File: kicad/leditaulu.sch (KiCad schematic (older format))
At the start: 45 parts, among them CON1 12V input, P1 Programming header, P2 I2C addr select, P4 I2C addr select, P5 Interconnect 1, P6 Interconnect 2, SW1 SW_SPST, SW2 SW_SPST, U1 ESP-12E, U2 TLC59116IPWR, U3 LD1086, U4 nRF24L01+, U5 TLC59116IPWR

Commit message: Fix submodules (ESP8266)
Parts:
- U1: footprint ESP8266:ESP-12E -> ESP8266:ESP-12E_SMD
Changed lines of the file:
@@
 F 0 "U1" H 2625 1350 50  0000 C CNN
 F 1 "ESP-12E" H 2625 1550 50  0000 C CNN
-F 2 "ESP8266:ESP-12E" H 2625 1450 50  0001 C CNN
+F 2 "ESP8266:ESP-12E_SMD" H 2625 1450 50  0001 C CNN
 F 3 "" H 2625 1450 50  0001 C CNN
 	1    2625 1450
@@
 ESP_GPIO0
 $Comp
-L Earth #PWR26
+L Earth #PWR01
 U 1 1 58EA62EF
 P 10375 1000
-F 0 "#PWR26" H 10375 750 50  0001 C CNN
+F 0 "#PWR01" H 10375 750 50  0001 C CNN
 F 1 "Earth" H 10375 850 50  0001 C CNN
 F 2 "" H 10375 1000 50  0000 C CNN
@@
 $EndComp
 $Comp
-L Earth #PWR27
+L Earth #PWR02
 U 1 1 58EA6329
 P 10375 1500
-F 0 "#PWR27" H 10375 1250 50  0001 C CNN
+F 0 "#PWR02" H 10375 1250 50  0001 C CNN
 F 1 "Earth" H 10375 1350 50  0001 C CNN
 F 2 "" H 10375 1500 50  0000 C CNN
@@
 3V3
 $Comp
-L Earth #PWR9
+L Earth #PWR03
 U 1 1 58EA6BBD
 P 3525 1850
-F 0 "#PWR9" H 3525 1600 50  0001 C CNN
+F 0 "#PWR03" H 3525 1600 50  0001 C CNN
 F 1 "Earth" H 3525 1700 50  0001 C CNN
 F 2 "" H 3525 1850 50  0000 C CNN
@@
 $EndComp
 $Comp
-L Earth #PWR5
+L Earth #PWR04
 U 1 1 58EA6CA7
 P 1200 2050
-F 0 "#PWR5" H 1200 1800 50  0001 C CNN
+F 0 "#PWR04" H 1200 1800 50  0001 C CNN
 F 1 "Earth" H 1200 1900 50  0001 C CNN
 F 2 "" H 1200 2050 50  0000 C CNN
@@
 $EndComp
 $Comp
-L Earth #PWR8
+L Earth #PWR05
 U 1 1 58EBE920
 P 2400 4300
-F 0 "#PWR8" H 2400 4050 50  0001 C CNN
+F 0 "#PWR05" H 2400 4050 50  0001 C CNN
 F 1 "Earth" H 2400 4150 50  0001 C CNN
 F 2 "" H 2400 4300 50  0000 C CNN
@@
 $EndComp
 $Comp
-L Earth #PWR11
+L Earth #PWR06
 U 1 1 58EBE9BE
 P 4100 3800
-F 0 "#PWR11" H 4100 3550 50  0001 C CNN
+F 0 "#PWR06" H 4100 3550 50  0001 C CNN
 F 1 "Earth" H 4100 3650 50  0001 C CNN
 F 2 "" H 4100 3800 50  0000 C CNN
@@
 $EndComp
 $Comp
-L Earth #PWR12
+L Earth #PWR07
 U 1 1 58EBE9F7
 P 4100 4300
-F 0 "#PWR12" H 4100 4050 50  0001 C CNN
+F 0 "#PWR07" H 4100 4050 50  0001 C CNN
 F 1 "Earth" H 4100 4150 50  0001 C CNN
 F 2 "" H 4100 4300 50  0000 C CNN
@@
 $EndComp
 $Comp
-L Earth #PWR13
+L Earth #PWR08
 U 1 1 58EBEB42
 P 4250 3075
-F 0 "#PWR13" H 4250 2825 50  0001 C CNN
+F 0 "#PWR08" H 4250 2825 50  0001 C CNN
 F 1 "Earth" H 4250 2925 50  0001 C CNN
 F 2 "" H 4250 3075 50  0000 C CNN
@@
 $EndComp
 $Comp
-L Earth #PWR7
+L Earth #PWR09
 U 1 1 58EBECB7
 P 2175 3200
-F 0 "#PWR7" H 2175 2950 50  0001 C CNN
+F 0 "#PWR09" H 2175 2950 50  0001 C CNN
 F 1 "Earth" H 2175 3050 50  0001 C CNN
 F 2 "" H 2175 3200 50  0000 C CNN
@@
 3V3
 $Comp
-L Earth #PWR1
+L Earth #PWR010
 U 1 1 58EBF732
 P 875 3500
-F 0 "#PWR1" H 875 3250 50  0001 C CNN
+F 0 "#PWR010" H 875 3250 50  0001 C CNN
 F 1 "Earth" H 875 3350 50  0001 C CNN
 F 2 "" H 875 3500 50  0000 C CNN
@@
 $EndComp
 $Comp
-L Earth #PWR2
+L Earth #PWR011
 U 1 1 58EBF764
 P 875 3600
-F 0 "#PWR2" H 875 3350 50  0001 C CNN
+F 0 "#PWR011" H 875 3350 50  0001 C CNN
 F 1 "Earth" H 875 3450 50  0001 C CNN
 F 2 "" H 875 3600 50  0000 C CNN
@@
 $EndComp
 $Comp
-L Earth #PWR3
+L Earth #PWR012
 U 1 1 58EBF796
 P 875 3700
-F 0 "#PWR3" H 875 3450 50  0001 C CNN
+F 0 "#PWR012" H 875 3450 50  0001 C CNN
 F 1 "Earth" H 875 3550 50  0001 C CNN
 F 2 "" H 875 3700 50  0000 C CNN
@@
 $EndComp
 $Comp
-L Earth #PWR4
+L Earth #PWR013
 U 1 1 58EBF7C8
 P 875 3800
-F 0 "#PWR4" H 875 3550 50  0001 C CNN
+F 0 "#PWR013" H 875 3550 50  0001 C CNN
 F 1 "Earth" H 875 3650 50  0001 C CNN
 F 2 "" H 875 3800 50  0000 C CNN
@@
 3V3
 $Comp
-L Earth #PWR6
+L Earth #PWR014
 U 1 1 58EC372D
 P 1950 6950
-F 0 "#PWR6" H 1950 6700 50  0001 C CNN
+F 0 "#PWR014" H 1950 6700 50  0001 C CNN
 F 1 "Earth" H 1950 6800 50  0001 C CNN
 F 2 "" H 1950 6950 50  0000 C CNN
@@
 VCC
 $Comp
-L Earth #PWR21
+L Earth #PWR015
 U 1 1 58EC41D8
 P 9425 1300
-F 0 "#PWR21" H 9425 1050 50  0001 C CNN
+F 0 "#PWR015" H 9425 1050 50  0001 C CNN
 F 1 "Earth" H 9425 1150 50  0001 C CNN
 F 2 "" H 9425 1300 50  0000 C CNN
@@
 $EndComp
 $Comp
-L Earth #PWR28
+L Earth #PWR016
 U 1 1 58EC54A0
 P 10375 2400
-F 0 "#PWR28" H 10375 2150 50  0001 C CNN
+F 0 "#PWR016" H 10375 2150 50  0001 C CNN
 F 1 "Earth" H 10375 2250 50  0001 C CNN
 F 2 "" H 10375 2400 50  0000 C CNN
@@
 $EndComp
 $Comp
-L Earth #PWR25
+L Earth #PWR017
 U 1 1 58ECFC8A
 P 9700 2400
-F 0 "#PWR25" H 9700 2150 50  0001 C CNN
+F 0 "#PWR017" H 9700 2150 50  0001 C CNN
 F 1 "Earth" H 9700 2250 50  0001 C CNN
 F 2 "" H 9700 2400 50  0000 C CNN
@@
 $EndComp
 $Comp
-L Earth #PWR20
+L Earth #PWR018
 U 1 1 58ED1380
 P 7775 4325
-F 0 "#PWR20" H 7775 4075 50  0001 C CNN
+F 0 "#PWR018" H 7775 4075 50  0001 C CNN
 F 1 "Earth" H 7775 4175 50  0001 C CNN
 F 2 "" H 7775 4325 50  0000 C CNN
@@
 $EndComp
 $Comp
-L Earth #PWR22
+L Earth #PWR019
 U 1 1 58ED1386
 P 9475 3825
-F 0 "#PWR22" H 9475 3575 50  0001 C CNN
+F 0 "#PWR019" H 9475 3575 50  0001 C CNN
 F 1 "Earth" H 9475 3675 50  0001 C CNN
 F 2 "" H 9475 3825 50  0000 C CNN
@@
 $EndComp
 $Comp
-L Earth #PWR23
+L Earth #PWR020
 U 1 1 58ED138C
 P 9475 4325
-F 0 "#PWR23" H 9475 4075 50  0001 C CNN
+F 0 "#PWR020" H 9475 4075 50  0001 C CNN
 F 1 "Earth" H 9475 4175 50  0001 C CNN
 F 2 "" H 9475 4325 50  0000 C CNN
@@
 $EndComp
 $Comp
-L Earth #PWR24
+L Earth #PWR021
 U 1 1 58ED1399
 P 9625 3100
-F 0 "#PWR24" H 9625 2850 50  0001 C CNN
+F 0 "#PWR021" H 9625 2850 50  0001 C CNN
 F 1 "Earth" H 9625 2950 50  0001 C CNN
 F 2 "" H 9625 3100 50  0000 C CNN
@@
 $EndComp
 $Comp
-L Earth #PWR19
+L Earth #PWR022
 U 1 1 58ED13A5
 P 7550 3225
-F 0 "#PWR19" H 7550 2975 50  0001 C CNN
+F 0 "#PWR022" H 7550 2975 50  0001 C CNN
 F 1 "Earth" H 7550 3075 50  0001 C CNN
 F 2 "" H 7550 3225 50  0000 C CNN
@@
 3V3
 $Comp
-L Earth #PWR15
+L Earth #PWR023
 U 1 1 58ED13CD
 P 6250 3525
-F 0 "#PWR15" H 6250 3275 50  0001 C CNN
+F 0 "#PWR023" H 6250 3275 50  0001 C CNN
 F 1 "Earth" H 6250 3375 50  0001 C CNN
 F 2 "" H 6250 3525 50  0000 C CNN
@@
 $EndComp
 $Comp
-L Earth #PWR16
+L Earth #PWR024
 U 1 1 58ED13D3
 P 6250 3625
-F 0 "#PWR16" H 6250 3375 50  0001 C CNN
+F 0 "#PWR024" H 6250 3375 50  0001 C CNN
 F 1 "Earth" H 6250 3475 50  0001 C CNN
 F 2 "" H 6250 3625 50  0000 C CNN
@@
 $EndComp
 $Comp
-L Earth #PWR17
+L Earth #PWR025
 U 1 1 58ED13D9
 P 6250 3725
-F 0 "#PWR17" H 6250 3475 50  0001 C CNN
+F 0 "#PWR025" H 6250 3475 50  0001 C CNN
 F 1 "Earth" H 6250 3575 50  0001 C CNN
 F 2 "" H 6250 3725 50  0000 C CNN
@@
 $EndComp
 $Comp
-L Earth #PWR18
+L Earth #PWR026
 U 1 1 58ED13DF
 P 6250 3825
-F 0 "#PWR18" H 6250 3575 50  0001 C CNN
+F 0 "#PWR026" H 6250 3575 50  0001 C CNN
 F 1 "Earth" H 6250 3675 50  0001 C CNN
 F 2 "" H 6250 3825 50  0000 C CNN
@@
 $EndComp
 $Comp
-L Earth #PWR14
+L Earth #PWR027
 U 1 1 58ED076D
 P 4250 6575
-F 0 "#PWR14" H 4250 6325 50  0001 C CNN
+F 0 "#PWR027" H 4250 6325 50  0001 C CNN
 F 1 "Earth" H 4250 6425 50  0001 C CNN
 F 2 "" H 4250 6575 50  0000 C CNN
@@
 $EndComp
 $Comp
-L Earth #PWR10
+L Earth #PWR028
 U 1 1 58ED6D4A
 P 4000 2225
-F 0 "#PWR10" H 4000 1975 50  0001 C CNN
+F 0 "#PWR028" H 4000 1975 50  0001 C CNN
 F 1 "Earth" H 4000 2075 50  0001 C CNN
 F 2 "" H 4000 2225 50  0000 C CNN
@@
 NoConn ~ 1725 1450
 $Comp
-L PWR_FLAG #FLG2
+L PWR_FLAG #FLG029
 U 1 1 5902A362
 P 1150 6925
-F 0 "#FLG2" H 1150 7020 50  0001 C CNN
+F 0 "#FLG029" H 1150 7020 50  0001 C CNN
 F 1 "PWR_FLAG" H 1150 7105 50  0000 C CNN
 F 2 "" H 1150 6925 50  0000 C CNN
@@
 $EndComp
 $Comp
-L PWR_FLAG #FLG1
+L PWR_FLAG #FLG030
 U 1 1 5902A2A8
 P 1150 6475
-F 0 "#FLG1" H 1150 6570 50  0001 C CNN
+F 0 "#FLG030" H 1150 6570 50  0001 C CNN
 F 1 "PWR_FLAG" H 1150 6655 50  0000 C CNN
 F 2 "" H 1150 6475 50  0000 C CNN
@@
 F 0 "SW1" H 6700 1275 50  0000 C CNN
 F 1 "SW_SPST" H 6700 1050 50  0000 C CNN
-F 2 "" H 6700 1150 50  0000 C CNN
+F 2 "" H 6700 1150 50  0001 C CNN
 F 3 "" H 6700 1150 50  0000 C CNN
 	1    6700 1150
@@
 F 0 "SW2" H 7350 1275 50  0000 C CNN
 F 1 "SW_SPST" H 7350 1050 50  0000 C CNN
-F 2 "" H 7350 1150 50  0000 C CNN
+F 2 "" H 7350 1150 50  0001 C CNN
 F 3 "" H 7350 1150 50  0000 C CNN
 	1    7350 1150

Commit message: Finish routing
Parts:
- added R19: 10K, Resistors_SMD:R_1206_HandSoldering, symbol R_Small
- SW1: value SW_SPST -> SW_RESET; footprint (none) -> Buttons_Switches_SMD:SW_SPST_B3S-1000
- SW2: value SW_SPST -> SW_FLASH; footprint (none) -> Buttons_Switches_SMD:SW_SPST_B3S-1000
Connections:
- net 3V3: now also R19.1
- net ESP_GPIO0: now also SW2.1 (A); no longer P1.2 (P2)
- net ESP_RST: now also SW1.1 (A), R19.2; no longer P1.3 (P3)
- net Earth: now also P1.2 (P2), SW1.2 (B), SW2.2 (B); no longer P1.6 (P6)
- no-connect marks 10 -> 12
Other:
- moved on the sheet: R1, SW1, SW2

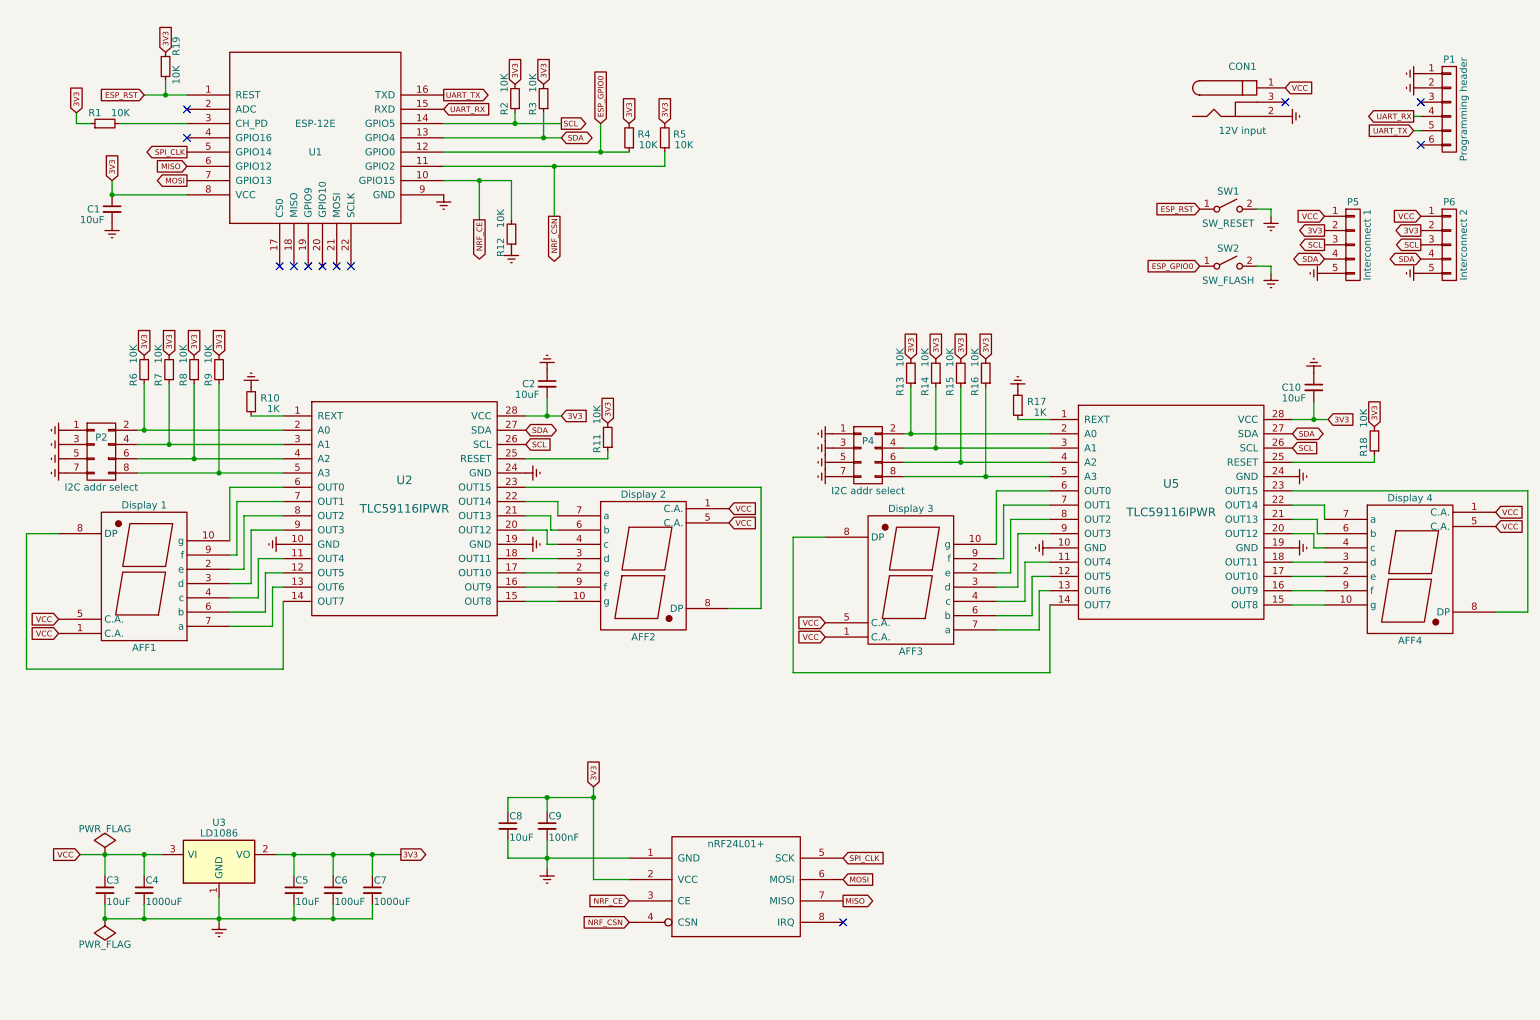
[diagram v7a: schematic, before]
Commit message: Add power supply protection; misc. fixes
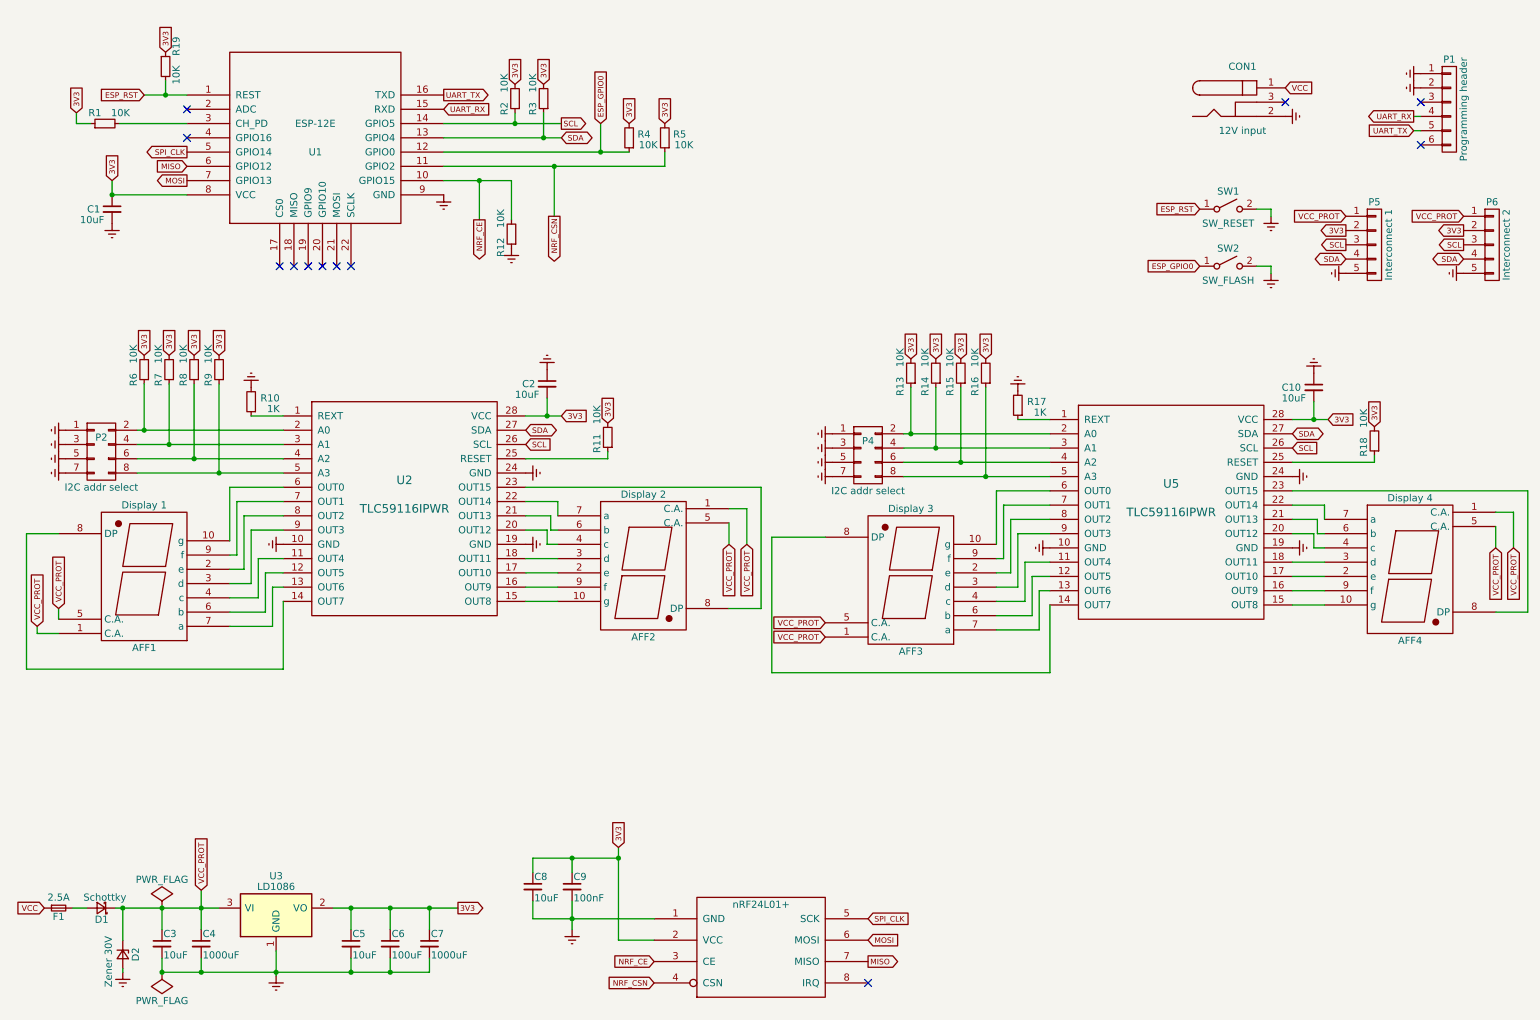
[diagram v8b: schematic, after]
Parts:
- added D1: Schottky, Diodes_SMD:D_SOD-123F, symbol D_Schottky_Small
- added D2: Zener 30V, Diodes_SMD:D_SMB_Handsoldering, symbol D_Zener_Small
- added F1: 2.5A, Resistors_SMD:R_0603_HandSoldering, symbol Fuse_Small
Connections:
- net Earth: now also D2.2 (A)
- net VCC: now also F1.1; no longer AFF1.1 (C.A.), AFF1.5 (C.A.), AFF2.1 (C.A.), AFF2.5 (C.A.), AFF3.1 (C.A.), AFF3.5 (C.A.), AFF4.1 (C.A.), AFF4.5 (C.A.), C3.1, C4.1, P5.1 (P1), P6.1 (P1), U3.3 (VI)
- new net: D1.2 (A), F1.2
- new net VCC_PROT: AFF1.1 (C.A.), AFF1.5 (C.A.), AFF2.1 (C.A.), AFF2.5 (C.A.), AFF3.1 (C.A.), AFF3.5 (C.A.), AFF4.1 (C.A.), AFF4.5 (C.A.), C3.1, C4.1, D1.1 (K), D2.1 (K), P5.1 (P1), P6.1 (P1), U3.3 (VI)
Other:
- moved on the sheet: C3, C4, C5, C6, C7, C8, C9, P5, P6, U3
